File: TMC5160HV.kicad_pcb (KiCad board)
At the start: 2 copper layers, 4 parts, among them IC1 TMC5160-TA, J1 825433-4, J2 825433-8, J3 825433-8

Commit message: Updates
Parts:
- added Q1: STL8DN10LF3, lib:STL50DN6F7, F.Cu at (114.3, 101.6)
- renumbered IC1 to U1
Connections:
- J2 pad 1: unconnected-(J2-Pad1) -> /EN
- J2 pad 2: unconnected-(J2-Pad2) -> /SDI
- J2 pad 3: unconnected-(J2-Pad3) -> /SCK
- J2 pad 4: unconnected-(J2-Pad4) -> /CSN
- J2 pad 5: unconnected-(J2-Pad5) -> /SDO
- J2 pad 6: unconnected-(J2-Pad6) -> /CLK
- J2 pad 7: unconnected-(J2-Pad7) -> /STEP
- J2 pad 8: unconnected-(J2-Pad8) -> /DIR
- J3 pad 1: unconnected-(J3-Pad1) -> /VM
- J3 pad 2: unconnected-(J3-Pad2) -> GND
- J3 pad 3: unconnected-(J3-Pad3) -> /BMA2
- J3 pad 4: unconnected-(J3-Pad4) -> /BMA1
- J3 pad 5: unconnected-(J3-Pad5) -> /BMB1
- J3 pad 6: unconnected-(J3-Pad6) -> /BMB2
- J3 pad 7: unconnected-(J3-Pad7) -> /VCCIO
- J3 pad 8: unconnected-(J3-Pad8) -> GND
- U1 pad 1: unconnected-(IC1-Pad1) -> /HB1
- U1 pad 10: unconnected-(IC1-Pad10) -> /SRBL
- U1 pad 11: unconnected-(IC1-Pad11) -> GND
- U1 pad 12: unconnected-(IC1-Pad12) -> /CLK
- U1 pad 13: unconnected-(IC1-Pad13) -> /CSN
- U1 pad 14: unconnected-(IC1-Pad14) -> /SCK
- U1 pad 15: unconnected-(IC1-Pad15) -> /SDL
- U1 pad 16: unconnected-(IC1-Pad16) -> /SDO
- U1 pad 17: unconnected-(IC1-Pad17) -> /STEP
- U1 pad 18: unconnected-(IC1-Pad18) -> /DIR
- U1 pad 19: unconnected-(IC1-Pad19) -> GND
- U1 pad 2: unconnected-(IC1-Pad2) -> /CBA1
- U1 pad 20: unconnected-(IC1-Pad20) -> /VCCIO
- U1 pad 21: unconnected-(IC1-Pad21) -> /VCCIO
- U1 pad 22: unconnected-(IC1-Pad22) -> /VCCIO
- U1 pad 26: unconnected-(IC1-Pad26) -> /DIAG0
- U1 pad 27: unconnected-(IC1-Pad27) -> /DIAG1
- U1 pad 28: unconnected-(IC1-Pad28) -> /DREN
- U1 pad 29: unconnected-(IC1-Pad29) -> Net-(U1-Pad29)
- U1 pad 3: unconnected-(IC1-Pad3) -> Net-(U1-Pad3)
- U1 pad 30: unconnected-(IC1-Pad30) -> GND
- U1 pad 31: unconnected-(IC1-Pad31) -> Net-(U1-Pad31)
- U1 pad 32: unconnected-(IC1-Pad32) -> Net-(U1-Pad32)
- U1 pad 33: unconnected-(IC1-Pad33) -> /VM
- U1 pad 34: unconnected-(IC1-Pad34) -> Net-(U1-Pad34)
- U1 pad 35: unconnected-(IC1-Pad35) -> /CA2
- U1 pad 36: unconnected-(IC1-Pad36) -> /HA2
- U1 pad 37: unconnected-(IC1-Pad37) -> /BMA2
- U1 pad 38: unconnected-(IC1-Pad38) -> /LA2
- U1 pad 39: unconnected-(IC1-Pad39) -> /LA1
- U1 pad 4: unconnected-(IC1-Pad4) -> /VM
- U1 pad 40: unconnected-(IC1-Pad40) -> /BMA1
- U1 pad 41: unconnected-(IC1-Pad41) -> /HA1
- U1 pad 42: unconnected-(IC1-Pad42) -> /CA1
- U1 pad 43: unconnected-(IC1-Pad43) -> /CB2
- U1 pad 44: unconnected-(IC1-Pad44) -> /HB2
- U1 pad 45: unconnected-(IC1-Pad45) -> /BMB2
- U1 pad 46: unconnected-(IC1-Pad46) -> /LB2
- U1 pad 47: unconnected-(IC1-Pad47) -> /LB1
- U1 pad 48: unconnected-(IC1-Pad48) -> /BMB1
- U1 pad 49: unconnected-(IC1-Pad49) -> GND
- U1 pad 5: unconnected-(IC1-Pad5) -> Net-(U1-Pad5)
- U1 pad 6: unconnected-(IC1-Pad6) -> GND
- U1 pad 7: unconnected-(IC1-Pad7) -> /SRAL
- U1 pad 8: unconnected-(IC1-Pad8) -> /SRAH
- U1 pad 9: unconnected-(IC1-Pad9) -> /SRBH

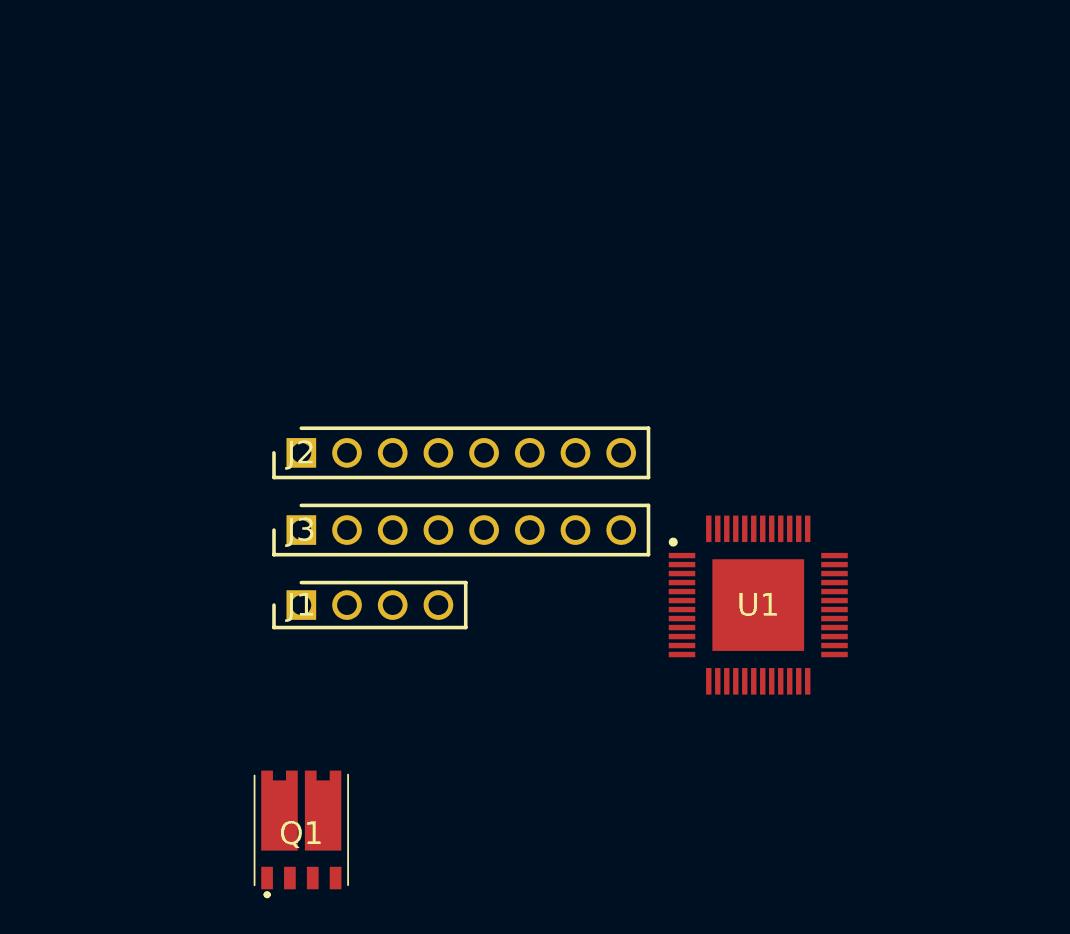
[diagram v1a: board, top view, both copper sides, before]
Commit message: 1206 for caps and 0603 for resistors
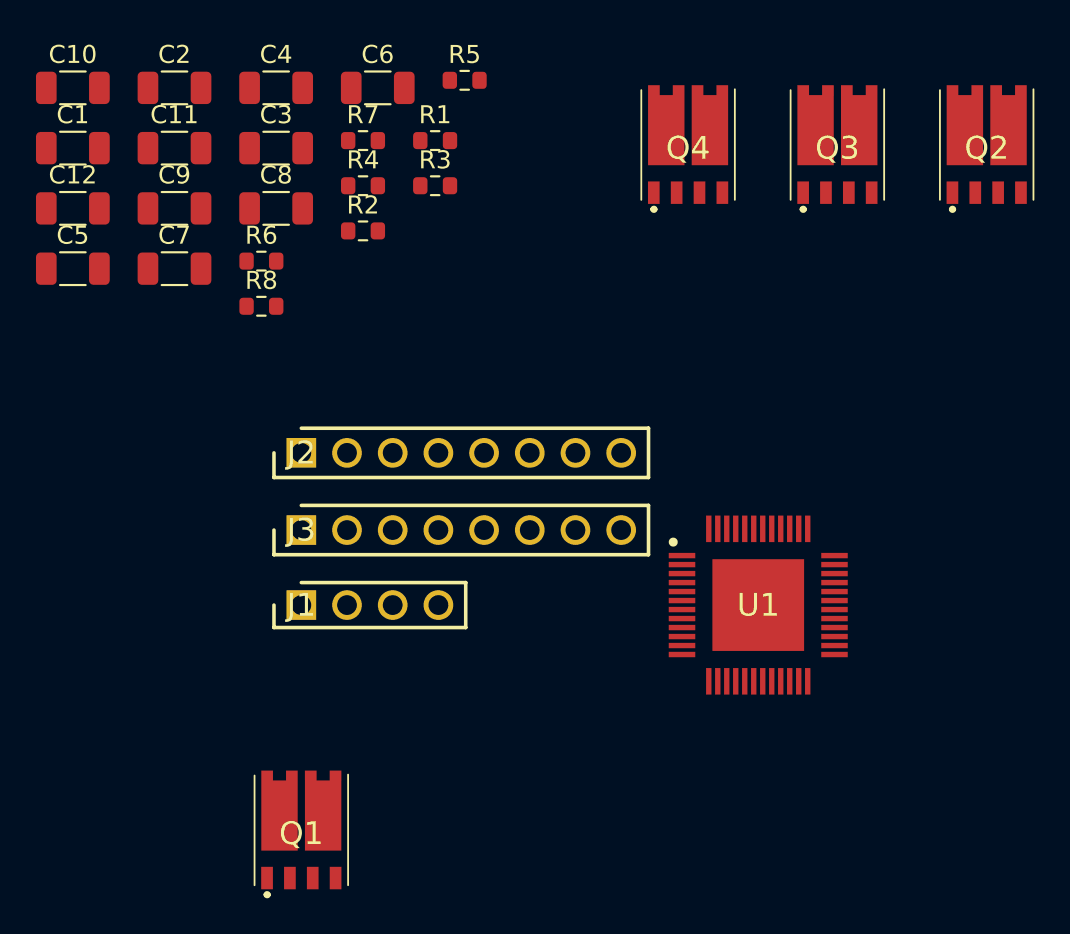
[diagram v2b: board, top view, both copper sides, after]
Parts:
- added C1: 2.2-10pF/100v, Capacitor_SMD:C_1206_3216Metric, F.Cu at (101.6, 63.5)
- added C10: 100nF/100V, Capacitor_SMD:C_1206_3216Metric, F.Cu at (101.6, 60.1)
- added C11: 470nF/100V, Capacitor_SMD:C_1206_3216Metric, F.Cu at (107.2, 63.5)
- added C12: 100nF/100V, Capacitor_SMD:C_1206_3216Metric, F.Cu at (101.6, 66.8)
- added C2: 100nF/100V, Capacitor_SMD:C_1206_3216Metric, F.Cu at (107.2, 60.1)
- added C3: 2.2-10pF/100v, Capacitor_SMD:C_1206_3216Metric, F.Cu at (112.9, 63.5)
- added C4: 100nF+, Capacitor_SMD:C_1206_3216Metric, F.Cu at (112.9, 60.1)
- added C5: 100nF/100V, Capacitor_SMD:C_1206_3216Metric, F.Cu at (101.6, 70.2)
- added C6: 22nF/100V, Capacitor_SMD:C_1206_3216Metric, F.Cu at (118.5, 60.1)
- added C7: 100nF/100V, Capacitor_SMD:C_1206_3216Metric, F.Cu at (107.2, 70.2)
- added C8: 100nF/100V, Capacitor_SMD:C_1206_3216Metric, F.Cu at (112.9, 66.8)
- added C9: 470nF/100V, Capacitor_SMD:C_1206_3216Metric, F.Cu at (107.2, 66.8)
- added Q2: STL8DN10LF3, lib:STL50DN6F7, F.Cu at (152.4, 63.5)
- added Q3: STL8DN10LF3, lib:STL50DN6F7, F.Cu at (144.1, 63.5)
- added Q4: STL8DN10LF3, lib:STL50DN6F7, F.Cu at (135.8, 63.5)
- added R1: 10k, Resistor_SMD:R_0603_1608Metric, F.Cu at (121.7, 63.1)
- added R2: 2.2k/+1%, Resistor_SMD:R_0603_1608Metric, F.Cu at (117.7, 68.1)
- added R3: 47R, Resistor_SMD:R_0603_1608Metric, F.Cu at (121.7, 65.6)
- added R4: 47R, Resistor_SMD:R_0603_1608Metric, F.Cu at (117.7, 65.6)
- added R5: 47R, Resistor_SMD:R_0603_1608Metric, F.Cu at (123.4, 59.7)
- added R6: 47R, Resistor_SMD:R_0603_1608Metric, F.Cu at (112.1, 69.8)
- added R7: 0.075R, Resistor_SMD:R_0603_1608Metric, F.Cu at (117.7, 63.1)
- added R8: 0.075R, Resistor_SMD:R_0603_1608Metric, F.Cu at (112.1, 72.3)
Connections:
- J1 pad 1: unconnected-(J1-Pad1) -> /DIAG0
- J1 pad 2: unconnected-(J1-Pad2) -> /DIAG1
- Q1 pad 1: unconnected-(Q1-Pad1) -> /BMB1
- Q1 pad 10: unconnected-(Q1-Pad10) -> /VM
- Q1 pad 2: unconnected-(Q1-Pad2) -> /HB2
- Q1 pad 3: unconnected-(Q1-Pad3) -> /BMB2
- Q1 pad 4: unconnected-(Q1-Pad4) -> /HB1
- Q1 pad 5: unconnected-(Q1-Pad5) -> /VM
- Q1 pad 6: unconnected-(Q1-Pad6) -> /VM
- Q1 pad 7: unconnected-(Q1-Pad7) -> /VM
- Q1 pad 8: unconnected-(Q1-Pad8) -> /VM
- Q1 pad 9: unconnected-(Q1-Pad9) -> /VM
